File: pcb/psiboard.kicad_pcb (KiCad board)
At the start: 2 copper layers, 99.6 x 64.5 mm, 11 parts, among them J2 BAT+, J3 BAT-

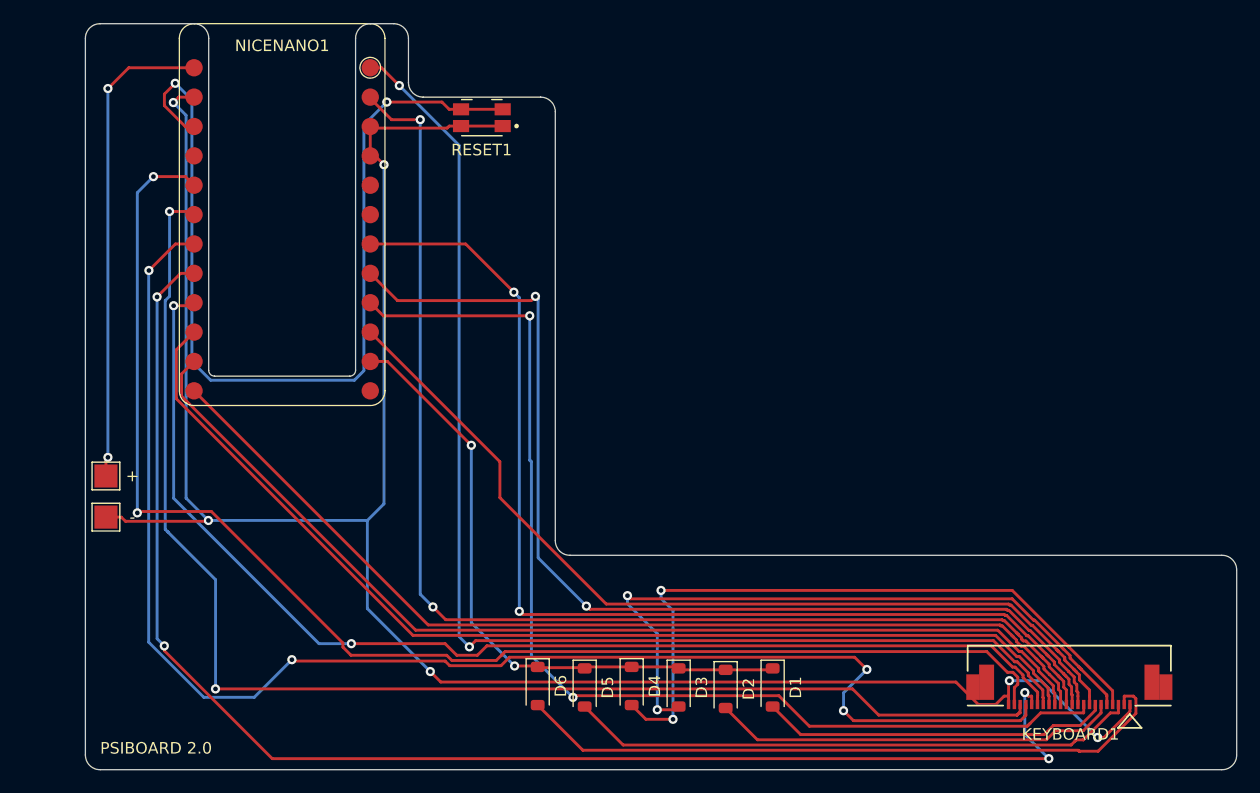
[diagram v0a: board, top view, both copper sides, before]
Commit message: Hand-route keyboard to simplify layout
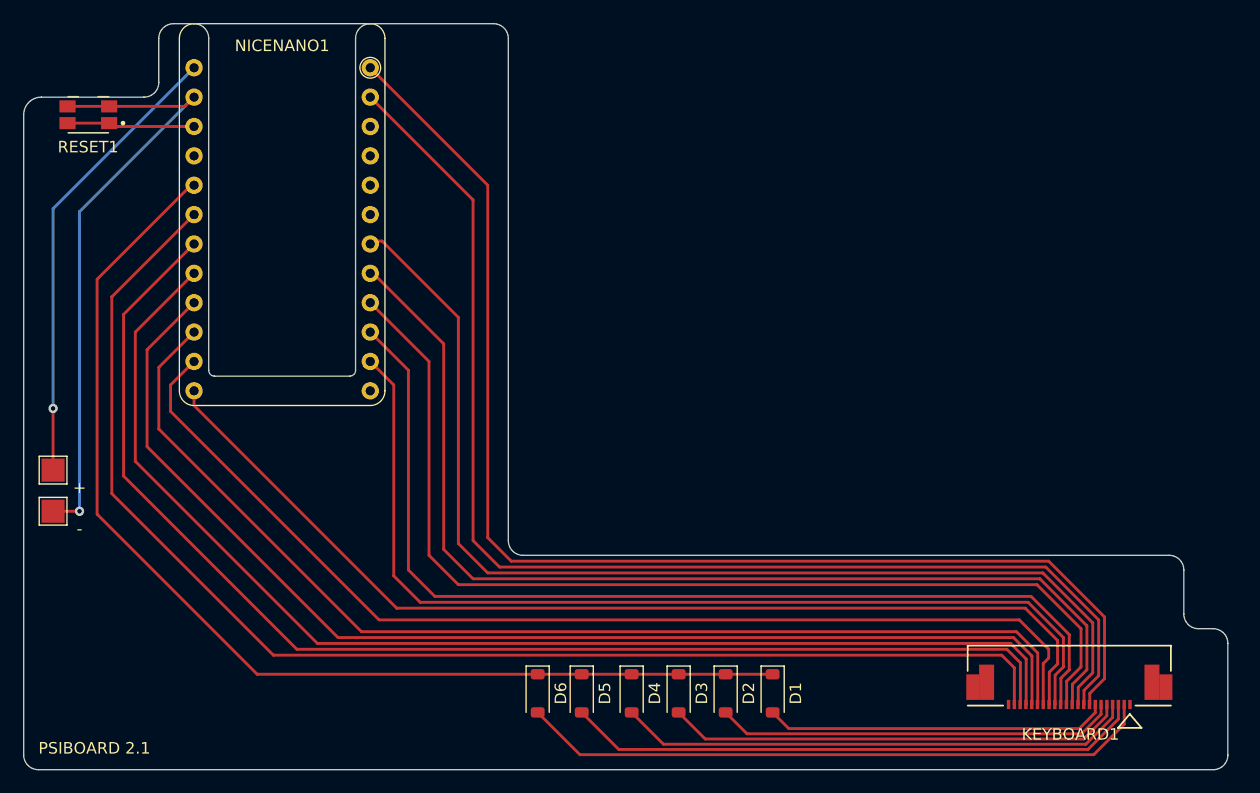
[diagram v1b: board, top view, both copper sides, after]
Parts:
- moved RESET1 34.0 mm to (80.3, 31.5)
- moved J2 4.60 mm to (77.2, 62.2)
- moved J3 4.60 mm to (77.2, 65.8)
- moved D4 0.64 mm to (127.3, 81.5)
- moved D6 0.63 mm to (119.1, 81.5)
- moved D5 0.57 mm to (122.9, 81.5)
- moved D1 0.51 mm to (139.4, 81.5)
- moved D3 0.51 mm to (131.3, 81.5)
- moved D2 0.38 mm to (135.4, 81.5)
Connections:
- KEYBOARD1 pad 1: GND -> unconnected-(KEYBOARD1-Pin_1-Pad1)
- KEYBOARD1 pad 22: GND -> unconnected-(KEYBOARD1-Pin_22-Pad22)
- NICENANO1 pad 1: ROW0 -> ROW5
- NICENANO1 pad 10: ROW5 -> COL7
- NICENANO1 pad 11: ROW6 -> COL6
- NICENANO1 pad 13: COL7 -> COL5
- NICENANO1 pad 14: COL6 -> ROW0
- NICENANO1 pad 15: COL5 -> COL4
- NICENANO1 pad 16: COL4 -> COL3
- NICENANO1 pad 17: COL3 -> COL2
- NICENANO1 pad 18: COL2 -> COL1
- NICENANO1 pad 19: COL1 -> COL0
- NICENANO1 pad 2: ROW1 -> ROW4
- NICENANO1 pad 20: COL0 -> ROW6
- NICENANO1 pad 3: GND -> unconnected-(NICENANO1-GND-Pad3)
- NICENANO1 pad 4: GND -> unconnected-(NICENANO1-GND-Pad4)
- NICENANO1 pad 7: ROW2 -> ROW3
- NICENANO1 pad 8: ROW3 -> ROW2
- NICENANO1 pad 9: ROW4 -> ROW1
- RESET1 pad 1_1: GND -> RST
- RESET1 pad 1_2: GND -> RST
- RESET1 pad 2_1: RST -> GND
- RESET1 pad 2_2: RST -> GND
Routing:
- net GND: track 192.5 -> 53.5 mm, vias 6 -> 1
- net RST: track 80.5 -> 11.1 mm, vias 2 -> 0
- net ROW6: track 55.0 -> 96.9 mm, vias 2 -> 0
- net ROW5: track 79.0 -> 109.1 mm
- net COL3: track 123.3 -> 102.4 mm, vias 4 -> 0
- net ROW6-3: track 59.4 -> 39.8 mm, vias 2 -> 0
- net COL2: track 125.0 -> 106.4 mm, vias 4 -> 0
- net ROW1: track 108.2 -> 90.0 mm, vias 2 -> 0
- net ROW6-4: track 59.7 -> 44.8 mm, vias 2 -> 0
- net ROW0: track 107.2 -> 94.6 mm, vias 2 -> 0
- net ROW4: track 95.8 -> 106.8 mm, vias 2 -> 0
- net COL1: track 117.2 -> 110.5 mm, vias 2 -> 0
- net COL6: track 91.0 -> 85.6 mm
- net COL0: track 119.2 -> 114.6 mm, vias 2 -> 0
- net ROW3: track 91.4 -> 95.3 mm, vias 2 -> 0
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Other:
- board size 99.6 x 64.5 mm -> 104.1 x 64.5 mm
- board text added: "PSIBOARD 2.1"
- board text removed: "PSIBOARD 2.0"

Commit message: Add ground plane
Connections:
- NICENANO1 pad 3: unconnected-(NICENANO1-GND-Pad3) -> GND
- NICENANO1 pad 4: unconnected-(NICENANO1-GND-Pad4) -> GND
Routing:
- net GND: track 53.5 -> 8.30 mm, vias 1 -> 2
- net RAW: vias 1 -> 0
- net RST: vias 0 -> 2
- added copper zone on B.Cu, net GND
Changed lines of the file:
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@@
 	(net 29 "unconnected-(KEYBOARD1-Pin_1-Pad1)")
 	(net 30 "unconnected-(KEYBOARD1-Pin_22-Pad22)")
-	(net 31 "unconnected-(NICENANO1-GND-Pad3)")
-	(net 32 "unconnected-(NICENANO1-GND-Pad4)")
 	(footprint "Diode_SMD:D_SOD-123"
 		(layer "F.Cu")
@@
 		)
 		(property "Value" "EVQ-P7A01P"
-			(at 5.3975 -2.54 0)
+			(at 0 4.064 0)
 			(layer "F.Fab")
 			(effects
@@
 		(sheetname "/")
 		(sheetfile "psiboard.kicad_sch")
-		(attr smd dnp)
+		(attr smd)
 		(fp_line
 			(start -8.89 15.24)
@@
 			(layers "*.Cu" "*.Mask")
 			(remove_unused_layers no)
-			(net 31 "unconnected-(NICENANO1-GND-Pad3)")
+			(net 26 "GND")
 			(pinfunction "GND")
-			(pintype "input+no_connect")
+			(pintype "input")
 		)
 		(pad "4" thru_hole circle
@@
 			(layers "*.Cu" "*.Mask")
 			(remove_unused_layers no)
-			(net 32 "unconnected-(NICENANO1-GND-Pad4)")
+			(net 26 "GND")
 			(pinfunction "GND")
-			(pintype "input+no_connect")
+			(pintype "input")
 		)
 		(pad "5" thru_hole circle
@@
 	)
 	(segment
-		(start 82.064 30.771)
-		(end 78.464 30.771)
+		(start 79.502 65.786)
+		(end 77.216 65.786)
 		(width 0.25)
 		(layer "F.Cu")
@@
 	)
 	(segment
-		(start 79.502 65.786)
-		(end 77.216 65.786)
+		(start 78.464 30.771)
+		(end 82.064 30.771)
 		(width 0.25)
 		(layer "F.Cu")
@@
 	)
 	(segment
-		(start 89.408 29.972)
-		(end 88.609 30.771)
+		(start 78.464 30.771)
+		(end 77.433 30.771)
 		(width 0.25)
 		(layer "F.Cu")
@@
 	)
 	(segment
-		(start 88.609 30.771)
-		(end 82.064 30.771)
+		(start 77.433 30.771)
+		(end 76.454 31.75)
 		(width 0.25)
 		(layer "F.Cu")
@@
 	)
 	(via
+		(at 76.454 31.75)
+		(size 0.8)
+		(drill 0.4)
+		(layers "F.Cu" "B.Cu")
+		(net 26)
+	)
+	(via
 		(at 79.502 65.786)
 		(size 0.8)
@@
 	)
 	(segment
-		(start 79.502 65.786)
-		(end 79.502 39.878)
+		(start 84.328 32.512)
+		(end 82.355 32.512)
 		(width 0.25)
-		(layer "B.Cu")
-		(net 26)
+		(layer "F.Cu")
+		(net 27)
 	)
 	(segment
-		(start 79.502 39.878)
-		(end 89.408 29.972)
+		(start 82.064 32.221)
+		(end 78.464 32.221)
 		(width 0.25)
-		(layer "B.Cu")
-		(net 26)
+		(layer "F.Cu")
+		(net 27)
 	)
 	(segment
@@
 	(segment
 		(start 89.408 32.512)
-		(end 82.355 32.512)
+		(end 87.376 32.512)
 		(width 0.25)
 		(layer "F.Cu")
 		(net 27)
 	)
+	(via
+		(at 84.328 32.512)
+		(size 0.8)
+		(drill 0.4)
+		(layers "F.Cu" "B.Cu")
+		(net 27)
+	)
+	(via
+		(at 87.376 32.512)
+		(size 0.8)
+		(drill 0.4)
+		(layers "F.Cu" "B.Cu")
+		(net 27)
+	)
 	(segment
-		(start 82.064 32.221)
-		(end 78.464 32.221)
+		(start 87.376 32.512)
+		(end 84.328 32.512)
 		(width 0.25)
-		(layer "F.Cu")
+		(layer "B.Cu")
 		(net 27)
 	)
 	(segment
-		(start 77.216 56.896)
+		(start 77.216 42.418)
 		(end 77.216 62.23)
 		(width 0.25)
@@
 		(net 28)
 	)
-	(via
-		(at 77.216 56.896)
-		(size 0.8)
-		(drill 0.4)
-		(layers "F.Cu" "B.Cu")
+	(segment
+		(start 85.852 33.782)
+		(end 77.216 42.418)
+		(width 0.25)
+		(layer "F.Cu")
 		(net 28)
 	)
 	(segment
-		(start 77.216 56.896)
-		(end 77.216 39.624)
+		(start 89.408 27.432)
+		(end 85.852 30.988)
 		(width 0.25)
-		(layer "B.Cu")
+		(layer "F.Cu")
 		(net 28)
 	)
 	(segment
-		(start 77.216 39.624)
-		(end 89.408 27.432)
+		(start 85.852 30.988)
+		(end 85.852 33.782)
 		(width 0.25)
-		(layer "B.Cu")
+		(layer "F.Cu")
 		(net 28)
 	)
+	(zone
+		(net 26)
+		(net_name "GND")
+		(layer "B.Cu")
+		(name "GND")
+		(hatch edge 0.5)
+		(connect_pads
+			(clearance 0.508)
+		)
+		(min_thickness 0.25)
+		(filled_areas_thickness no)
+		(fill yes
+			(thermal_gap 0.5)
+			(thermal_bridge_width 0.5)
+			(smoothing fillet)
+			(radius 1)
+		)
+		(polygon
+			(pts
+				(xy 90.17 24.13) (xy 86.868 24.13) (xy 86.868 30.479928) (xy 75.183918 30.483241) (xy 75.165522 87.633313)
+				(xy 178.308 87.633313) (xy 178.308 76.457313) (xy 174.498 76.457313) (xy 174.498 70.104) (xy 116.078 70.103999)
+				(xy 116.078 24.133313) (xy 103.886 24.133313) (xy 103.886 54.613313) (xy 90.17 54.613313)
+			)
+		)
+	)
 	(embedded_fonts no)
